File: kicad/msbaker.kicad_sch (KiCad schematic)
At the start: 37 parts, among them J1 USB_B_Micro, J2 Micro_SD_Card, J3 GPIO, U1 MIC5365-3.3YC5, U2 W25Q128JVS, U3 RP2040, U4 LSM6DSO32, Y1 12MHz

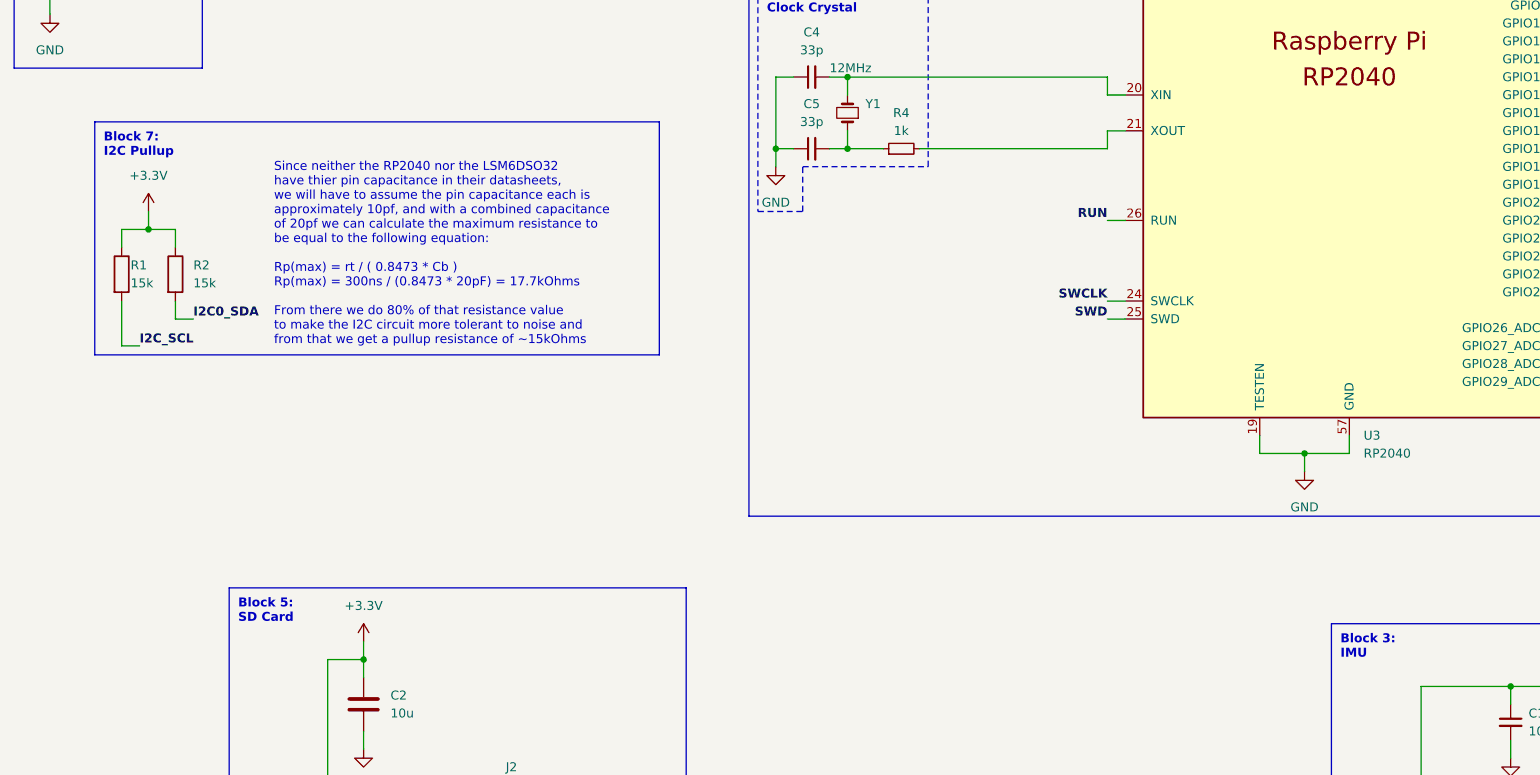
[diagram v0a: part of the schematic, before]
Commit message: Corrected block numbers
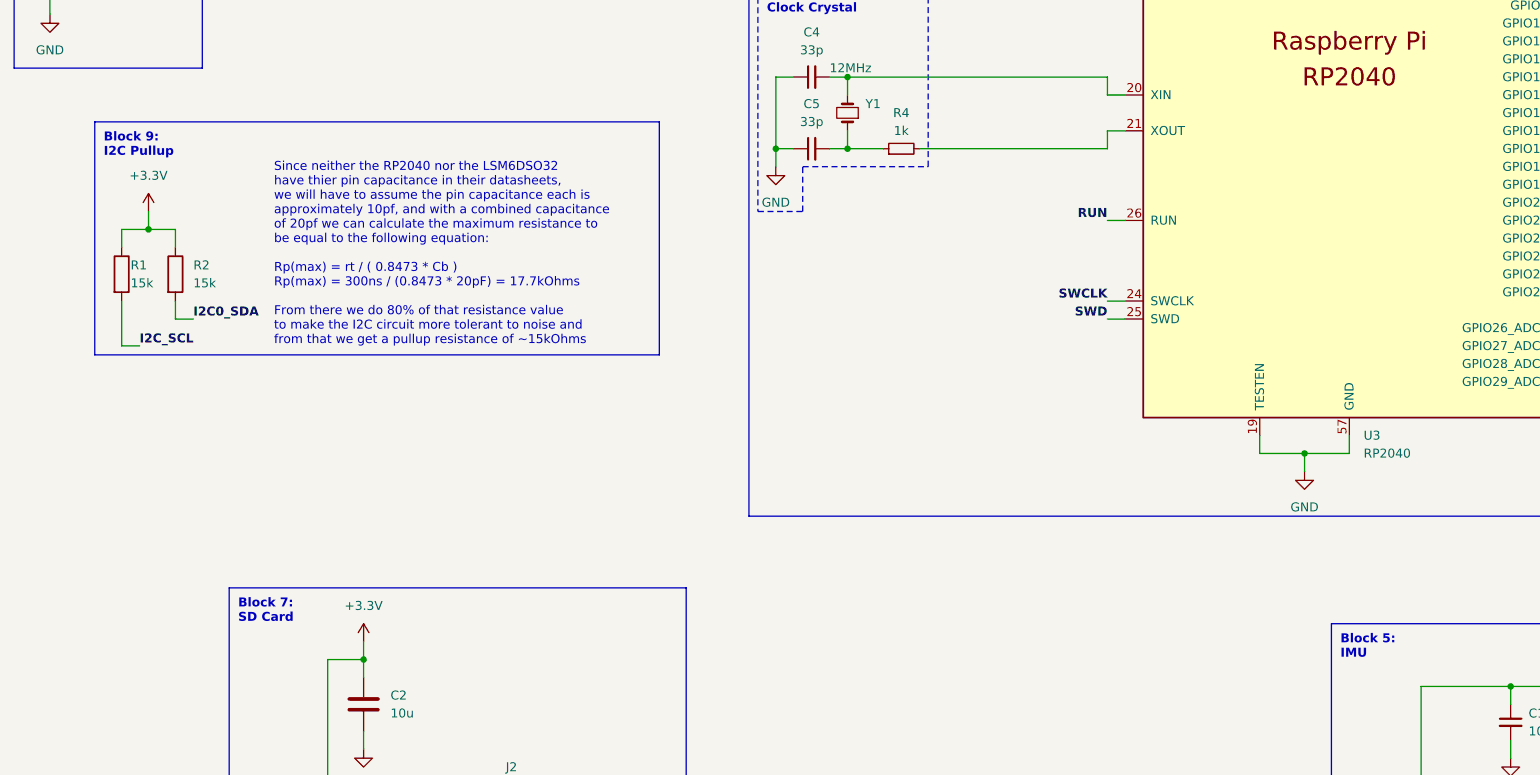
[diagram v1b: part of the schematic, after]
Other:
- note added: "Block 5: IMU"
- note added: "Block 7: SD Card"
- note added: "Block 9: I2C Pullup"
- note removed: "Block 3: IMU"
- note removed: "Block 5: SD Card"
- note removed: "Block 7: I2C Pullup"
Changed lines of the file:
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@@
     (effects (font (size 1.27 1.27) bold) (justify left bottom))
   )
-  (text "Block 3:\nIMU" (at 220.98 215.9 0)
+  (text "Block 5:\nIMU" (at 220.98 215.9 0)
     (effects (font (size 1.27 1.27) bold) (justify left bottom))
   )
@@
     (effects (font (size 1.27 1.27) bold) (justify left bottom))
   )
-  (text "Block 5:\nSD Card" (at 64.77 210.82 0)
+  (text "Block 7:\nSD Card" (at 64.77 210.82 0)
     (effects (font (size 1.27 1.27) bold) (justify left bottom))
   )
-  (text "Block 7:\nI2C Pullup" (at 45.72 144.78 0)
+  (text "Block 9:\nI2C Pullup" (at 45.72 144.78 0)
     (effects (font (size 1.27 1.27) bold) (justify left bottom))
   )

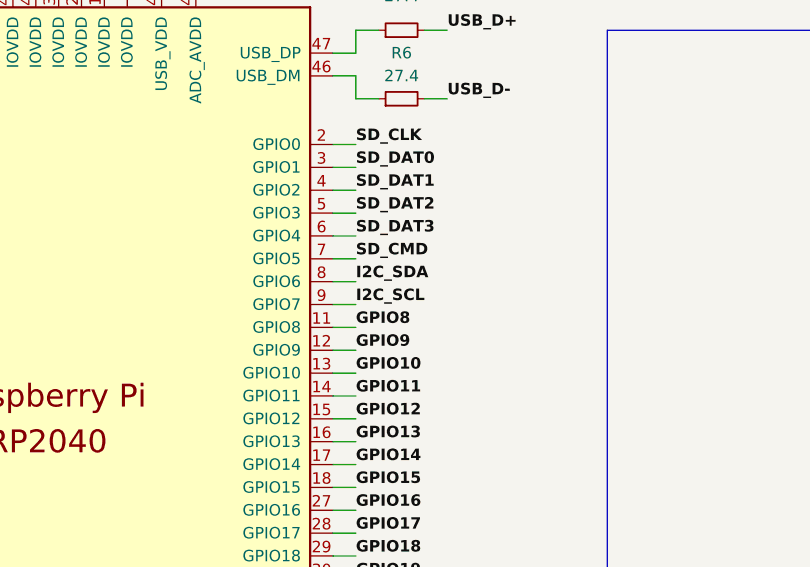
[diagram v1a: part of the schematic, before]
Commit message: Fixed typo in schematic
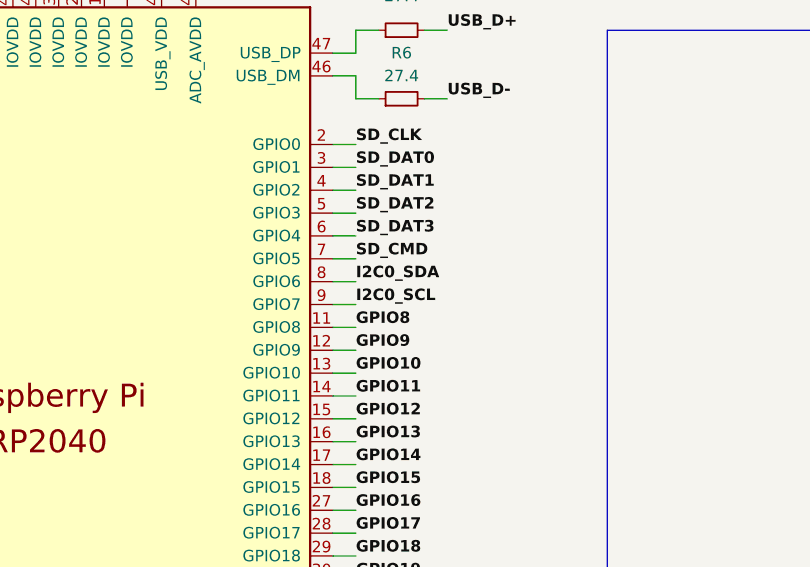
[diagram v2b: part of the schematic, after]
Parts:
- U3: footprint RP2040_minimal:RP2040-QFN-56 -> msbaker:RP2040-QFN-56
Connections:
- net I2C_SDA is gone; now on net I2C0_SDA: U3.8 (GPIO6)
- net I2C0_SCL: now also U3.9 (GPIO7)
- net I2C_SCL: no longer U3.9 (GPIO7)
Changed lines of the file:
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@@
     (effects (font (size 1.27 1.27) bold) (justify right bottom))
   )
-  (label "I2C_SCL" (at 256.54 118.11 0)
+  (label "I2C0_SCL" (at 256.54 118.11 0)
     (effects (font (size 1.27 1.27) bold) (justify left bottom))
   )
@@
     (effects (font (size 1.27 1.27) bold) (justify left bottom))
   )
-  (label "I2C_SDA" (at 256.54 115.57 0)
+  (label "I2C0_SDA" (at 256.54 115.57 0)
     (effects (font (size 1.27 1.27) bold) (justify left bottom))
   )
@@
       (effects (font (size 1.27 1.27)) (justify left))
     )
-    (property "Footprint" "RP2040_minimal:RP2040-QFN-56" (id 2) (at 203.2 133.35 0)
+    (property "Footprint" "msbaker:RP2040-QFN-56" (id 2) (at 203.2 133.35 0)
       (effects (font (size 1.27 1.27)) hide)
     )
@@
     )
     (path "/a530eb3b-850c-4348-9c18-72b32f461f6b"
-      (reference "U3") (unit 1) (value "RP2040") (footprint "RP2040_minimal:RP2040-QFN-56")
+      (reference "U3") (unit 1) (value "RP2040") (footprint "msbaker:RP2040-QFN-56")
     )
     (path "/9a16b67b-1f3d-4692-985a-7f1fc616b1b8"

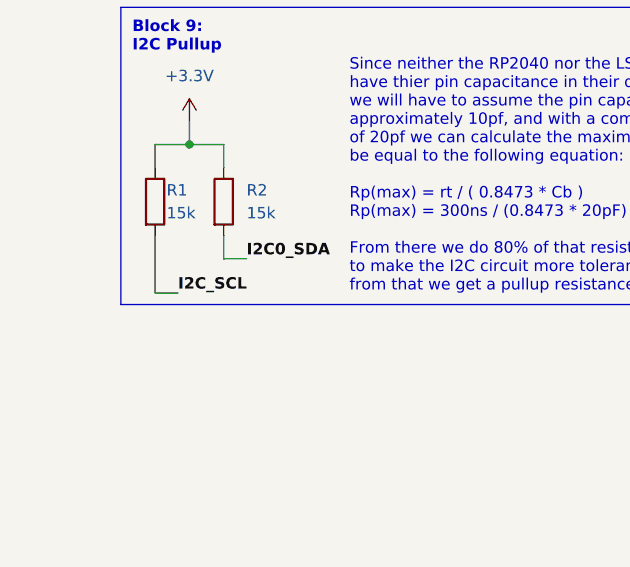
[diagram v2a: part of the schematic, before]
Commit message: Added pcb files
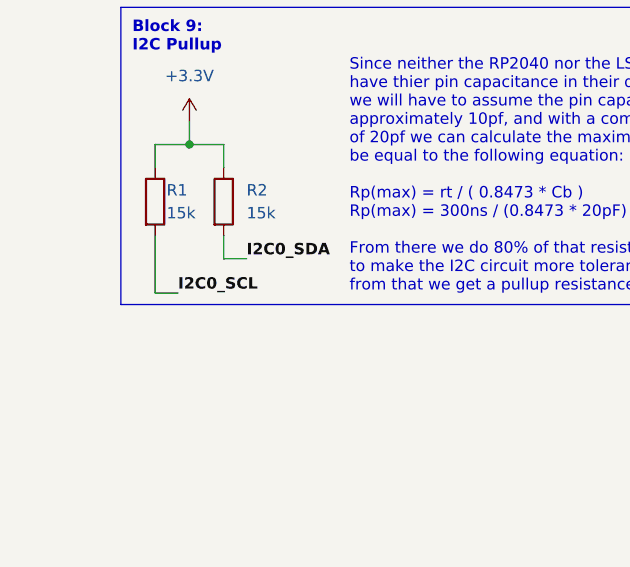
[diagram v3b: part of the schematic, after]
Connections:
- net I2C_SCL is gone; now on net I2C0_SCL: R1.2
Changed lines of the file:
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@@
     (effects (font (size 1.27 1.27) bold) (justify right bottom))
   )
-  (label "I2C_SCL" (at 50.8 171.45 0)
+  (label "I2C0_SCL" (at 50.8 171.45 0)
     (effects (font (size 1.27 1.27) bold) (justify left bottom))
   )

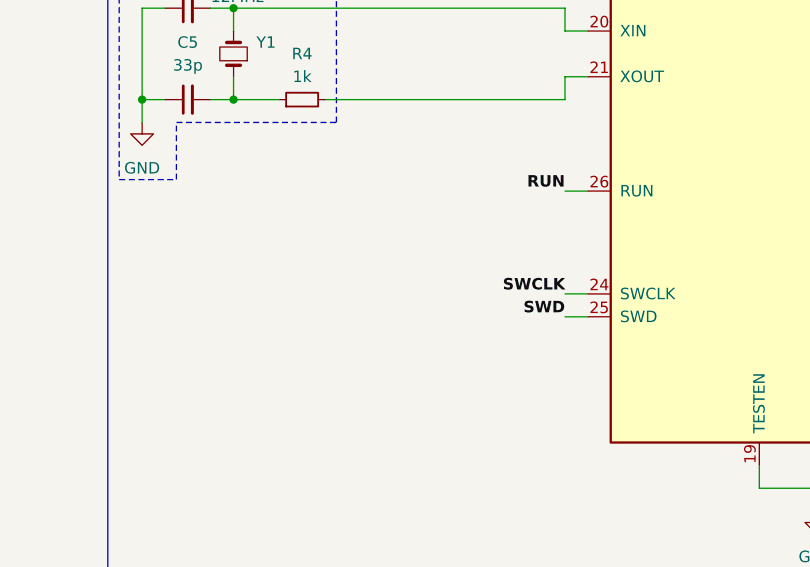
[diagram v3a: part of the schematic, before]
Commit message: Added reset jumper block
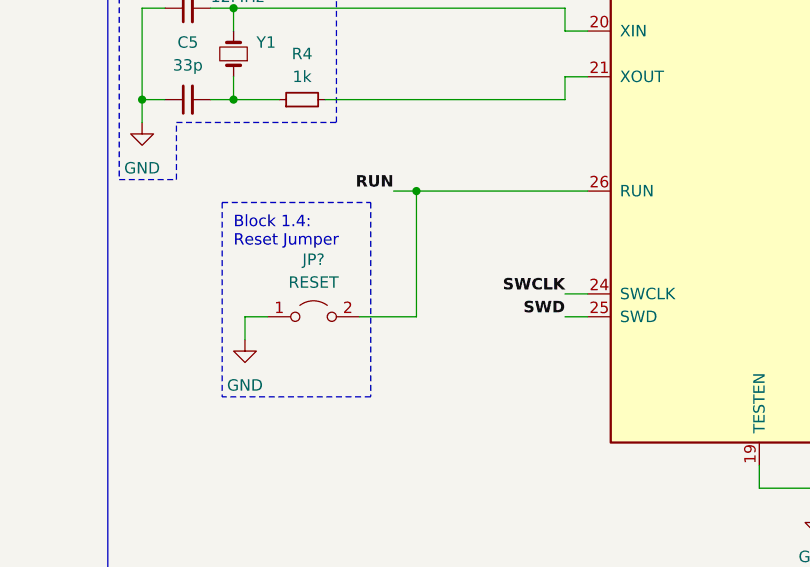
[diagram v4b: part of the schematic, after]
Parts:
- added JP?: RESET, symbol Jumper:Jumper_2_Open
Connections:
- net GND: now also JP?.1 (A)
- net RUN: now also JP?.2 (B)
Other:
- note added: "Block 1.4: Reset Jumper"
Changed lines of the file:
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@@
     (rev "3")
+  )
+  (junction (at 171.45 153.67) (diameter 0) (color 0 0 0 0)
   )
   (junction (at 38.1 121.92) (diameter 0) (color 0 0 0 0)
@@
     (stroke (width 0) (type default) (color 0 0 0 0))
   )
+  (wire (pts (xy 168.91 153.67) (xy 171.45 153.67))
+    (stroke (width 0) (type default) (color 0 0 0 0))
+  )
   (wire (pts (xy 261.62 74.93) (xy 261.62 77.47))
     (stroke (width 0) (type default) (color 0 0 0 0))
@@
     (stroke (width 0) (type default) (color 0 0 0 0))
   )
+  (polyline (pts (xy 166.37 154.94) (xy 166.37 176.53))
+    (stroke (width 0) (type dot) (color 0 0 0 0))
+  )
   (wire (pts (xy 349.25 157.48) (xy 354.33 157.48))
+    (stroke (width 0) (type default) (color 0 0 0 0))
+  )
+  (wire (pts (xy 171.45 153.67) (xy 190.5 153.67))
     (stroke (width 0) (type default) (color 0 0 0 0))
   )
@@
     (stroke (width 0) (type default) (color 0 0 0 0))
   )
+  (wire (pts (xy 152.4 167.64) (xy 152.4 170.18))
+    (stroke (width 0) (type default) (color 0 0 0 0))
+  )
   (wire (pts (xy 132.08 107.95) (xy 149.86 107.95))
     (stroke (width 0) (type default) (color 0 0 0 0))
@@
     (stroke (width 0) (type default) (color 0 0 0 0))
   )
+  (wire (pts (xy 171.45 153.67) (xy 171.45 167.64))
+    (stroke (width 0) (type default) (color 0 0 0 0))
+  )
+  (wire (pts (xy 171.45 167.64) (xy 165.1 167.64))
+    (stroke (width 0) (type default) (color 0 0 0 0))
+  )
   (wire (pts (xy 161.29 143.51) (xy 187.96 143.51))
     (stroke (width 0) (type default) (color 0 0 0 0))
@@
     (stroke (width 0) (type default) (color 0 0 0 0))
   )
+  (wire (pts (xy 154.94 167.64) (xy 152.4 167.64))
+    (stroke (width 0) (type default) (color 0 0 0 0))
+  )
   (wire (pts (xy 254 133.35) (xy 256.54 133.35))
     (stroke (width 0) (type default) (color 0 0 0 0))
@@
     (stroke (width 0) (type default) (color 0 0 0 0))
   )
-  (wire (pts (xy 187.96 153.67) (xy 190.5 153.67))
-    (stroke (width 0) (type default) (color 0 0 0 0))
-  )
   (wire (pts (xy 132.08 99.06) (xy 132.08 107.95))
     (stroke (width 0) (type default) (color 0 0 0 0))
@@
     (stroke (width 0) (type default) (color 0 0 0 0))
   )
+  (polyline (pts (xy 149.86 154.94) (xy 166.37 154.94))
+    (stroke (width 0) (type dot) (color 0 0 0 0))
+  )
   (wire (pts (xy 127 93.98) (xy 129.54 93.98))
     (stroke (width 0) (type default) (color 0 0 0 0))
@@
   (wire (pts (xy 255.27 266.7) (xy 252.73 266.7))
     (stroke (width 0) (type default) (color 0 0 0 0))
+  )
+  (polyline (pts (xy 149.86 154.94) (xy 149.86 176.53))
+    (stroke (width 0) (type dot) (color 0 0 0 0))
   )
   (wire (pts (xy 234.95 246.38) (xy 237.49 246.38))
@@
   (wire (pts (xy 297.18 74.93) (xy 297.18 77.47))
     (stroke (width 0) (type default) (color 0 0 0 0))
+  )
+  (polyline (pts (xy 166.37 176.53) (xy 149.86 176.53))
+    (stroke (width 0) (type dot) (color 0 0 0 0))
   )
   (wire (pts (xy 213.36 58.42) (xy 213.36 59.69))
@@
     (effects (font (size 1.27 1.27) bold) (justify left bottom))
   )
+  (text "Block 1.4:\nReset Jumper" (at 151.13 160.02 0)
+    (effects (font (size 1.27 1.27)) (justify left bottom))
+  )
   (label "GPIO15" (at 256.54 138.43 0)
     (effects (font (size 1.27 1.27) bold) (justify left bottom))
@@
     (effects (font (size 1.27 1.27) bold) (justify left bottom))
   )
-  (label "RUN" (at 187.96 153.67 180)
+  (label "RUN" (at 168.91 153.67 180)
     (effects (font (size 1.27 1.27) bold) (justify right bottom))
   )
@@
     (pin "2")
   )
+  (symbol (lib_id "Jumper:Jumper_2_Open") (at 160.02 167.64 0) (unit 1)
+    (in_bom yes) (on_board yes) (fields_autoplaced)
+    (property "Reference" "JP?" (id 0) (at 160.02 161.29 0))
+    (property "Value" "RESET" (id 1) (at 160.02 163.83 0))
+    (property "Footprint" "" (id 2) (at 160.02 167.64 0)
+      (effects (font (size 1.27 1.27)) hide)
+    )
+    (property "Datasheet" "~" (id 3) (at 160.02 167.64 0)
+      (effects (font (size 1.27 1.27)) hide)
+    )
+    (pin "1")
+    (pin "2")
+  )
   (symbol (lib_id "power:+5V") (at 68.58 40.64 0) (unit 1)
     (in_bom yes) (on_board yes) (fields_autoplaced)
@@
     (pin "1")
     (pin "2")
+  )
+  (symbol (lib_id "power:GND") (at 152.4 170.18 0) (unit 1)
+    (in_bom yes) (on_board yes) (fields_autoplaced)
+    (property "Reference" "#PWR?" (id 0) (at 152.4 176.53 0)
+      (effects (font (size 1.27 1.27)) hide)
+    )
+    (property "Value" "GND" (id 1) (at 152.4 175.26 0))
+    (property "Footprint" "" (id 2) (at 152.4 170.18 0)
+      (effects (font (size 1.27 1.27)) hide)
+    )
+    (property "Datasheet" "" (id 3) (at 152.4 170.18 0)
+      (effects (font (size 1.27 1.27)) hide)
+    )
+    (pin "1")
   )
   (symbol (lib_id "Device:C_Small") (at 146.05 133.35 90) (unit 1)
@@
       (reference "#PWR0127") (unit 1) (value "GND") (footprint "")
     )
+    (path "/34075927-0940-4a51-b071-f748f1aafb45"
+      (reference "#PWR?") (unit 1) (value "GND") (footprint "")
+    )
     (path "/c7da6979-49ad-4486-80d0-67dcc8e8ab59"
       (reference "C1") (unit 1) (value "1u") (footprint "Capacitor_SMD:C_0402_1005Metric")
@@
       (reference "JP1") (unit 1) (value "BOOTSEL") (footprint "Connector_PinHeader_2.54mm:PinHeader_1x02_P2.54mm_Vertical")
     )
+    (path "/23378ab5-1c12-4850-a758-87df6c952ed0"
+      (reference "JP?") (unit 1) (value "RESET") (footprint "")
+    )
     (path "/21a3236e-0675-438d-b524-ddd5ec5a0139"
